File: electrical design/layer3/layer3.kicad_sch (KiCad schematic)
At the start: 10 parts, among them U1 TEENSY 4.0

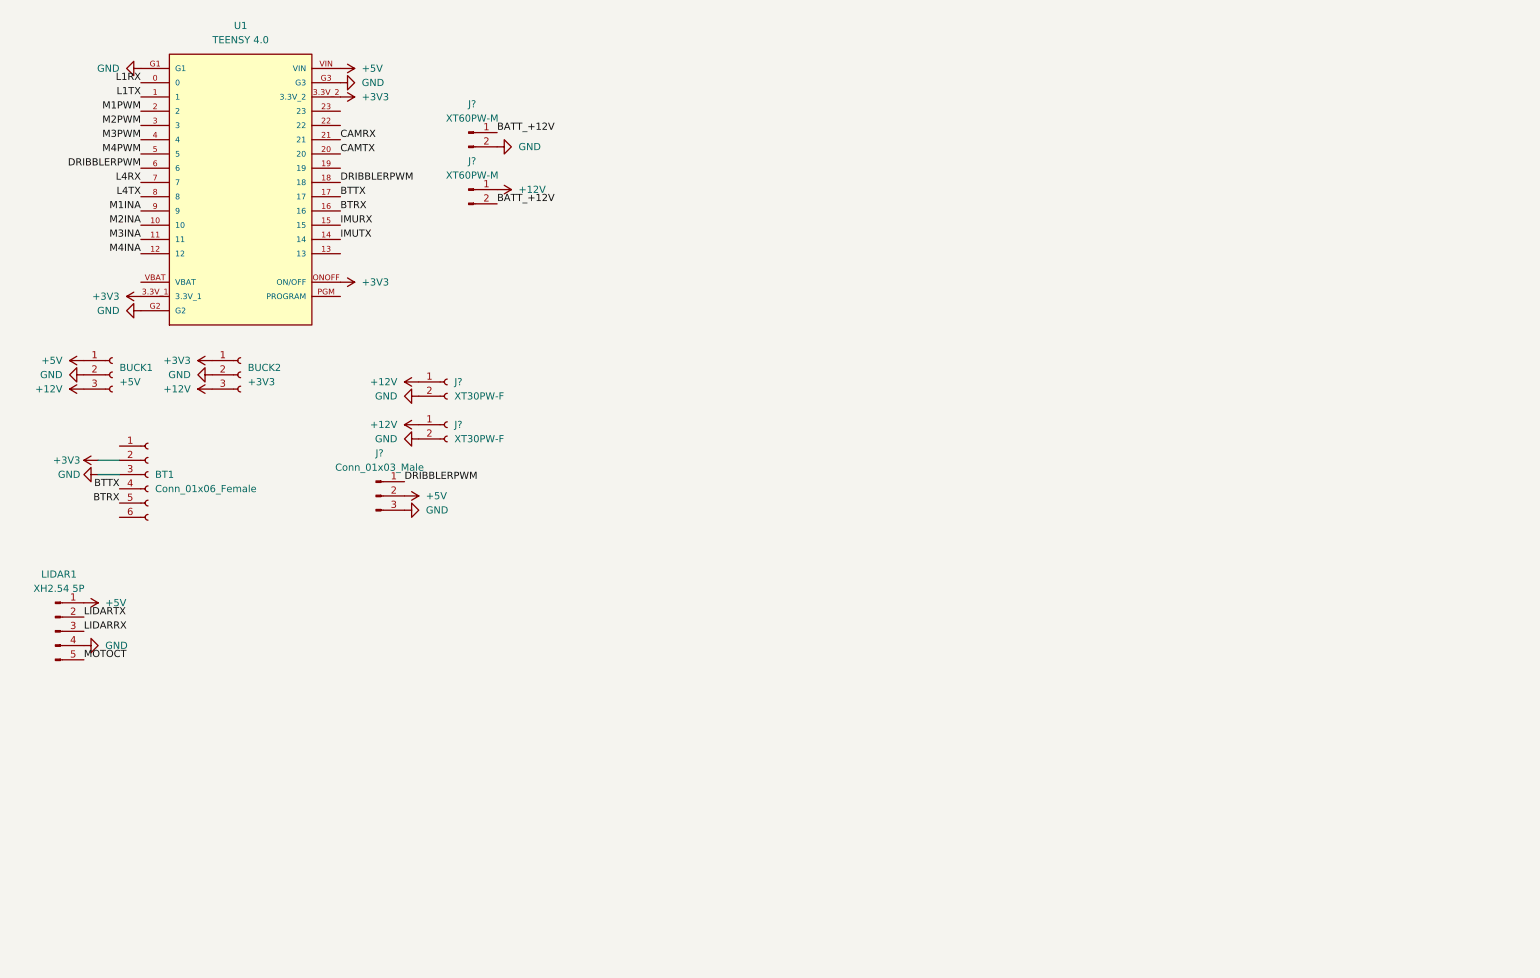
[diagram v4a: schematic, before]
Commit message: almost final layer 3 pcb design
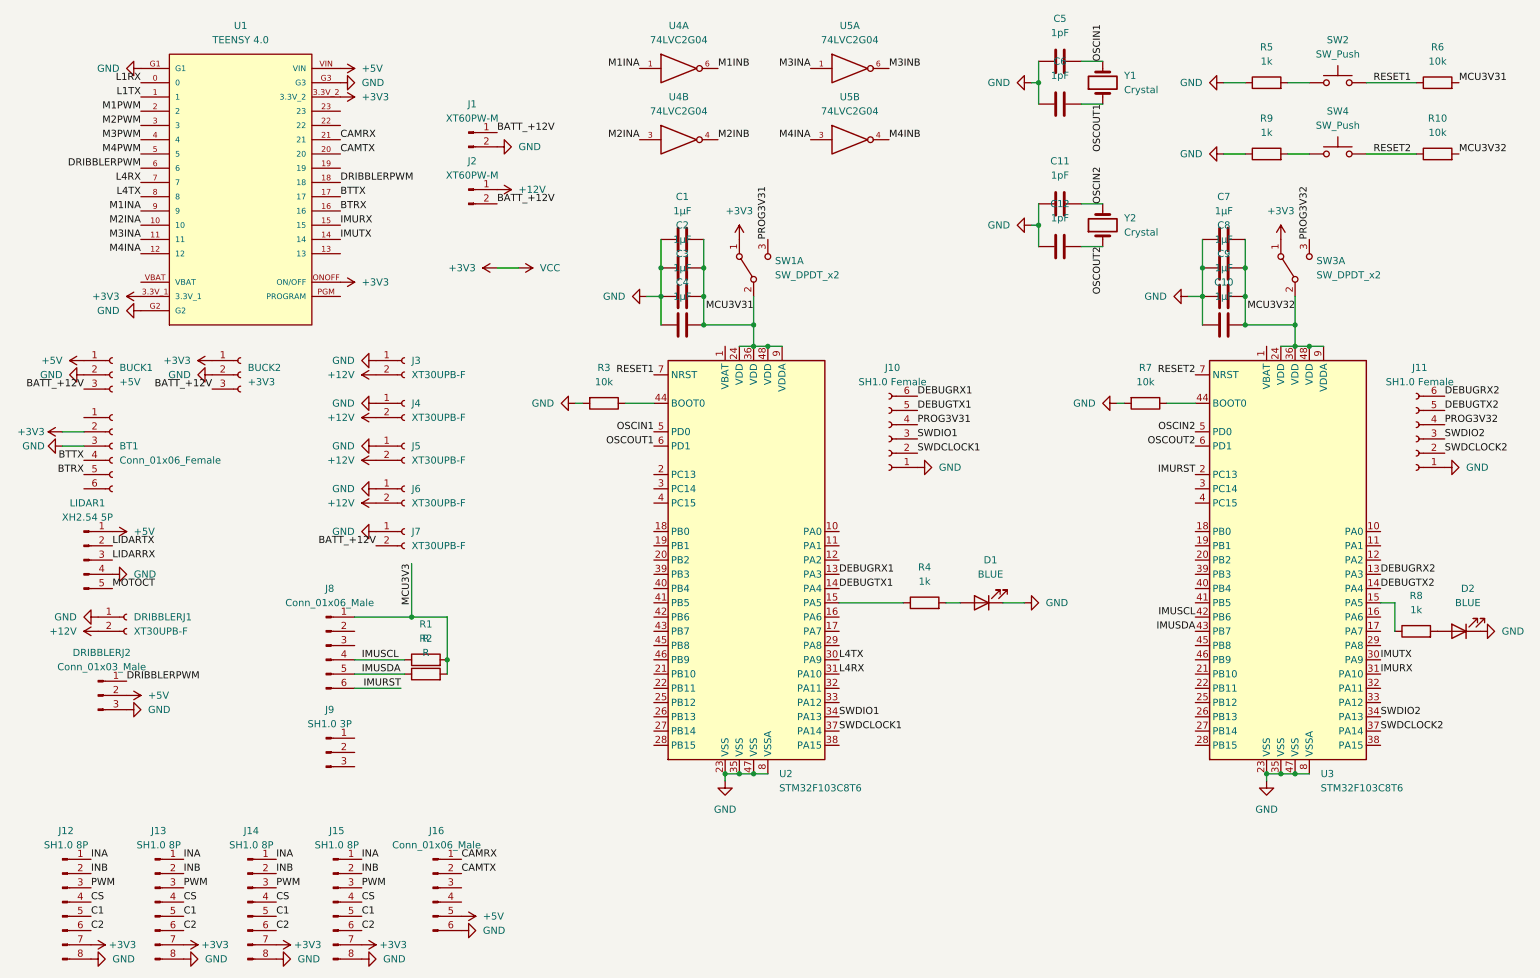
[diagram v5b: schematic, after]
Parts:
- removed J?: XT30PW-F, symbol Connector:Conn_01x02_Female
- added C1, C10, C2, C3, C4, C7, C8, C9: 1μF, Capacitor_SMD:C_0603_1608Metric, symbol Device:C
- added C11, C12, C5, C6: 1pF, Capacitor_SMD:C_0603_1608Metric, symbol Device:C
- added D1, D2: BLUE, Diode_SMD:D_0603_1608Metric, symbol Device:LED
- added J10, J11: SH1.0 Female, Connector_JST:JST_SH_BM06B-SRSS-TB_1x06-1MP_P1.00mm_Vertical, symbol Connector:Conn_01x06_Female
- added J12, J13, J14, J15: SH1.0 8P, Connector_JST:JST_SH_BM08B-SRSS-TB_1x08-1MP_P1.00mm_Vertical, symbol Connector:Conn_01x08_Male
- added J16: Conn_01x06_Male, Connector_JST:JST_GH_SM06B-GHS-TB_1x06-1MP_P1.25mm_Horizontal, symbol Connector:Conn_01x06_Male
- added J3, J4, J5, J6, J7: XT30UPB-F, Connector_AMASS:AMASS_XT30UPB-F_1x02_P5.0mm_Vertical, symbol Connector:Conn_01x02_Female
- added J8: Conn_01x06_Male, Connector_PinHeader_2.54mm:PinHeader_1x06_P2.54mm_Vertical, symbol Connector:Conn_01x06_Male
- added J9: SH1.0 3P, Connector_JST:JST_SH_SM03B-SRSS-TB_1x03-1MP_P1.00mm_Horizontal, symbol Connector:Conn_01x03_Male
- added R1, R2: R, Resistor_SMD:R_0603_1608Metric, symbol Device:R
- added R10, R3, R6, R7: 10k, Resistor_SMD:R_0603_1608Metric, symbol Device:R
- added R4, R5, R8, R9: 1k, Resistor_SMD:R_0603_1608Metric, symbol Device:R
- added SW1, SW3: SW_DPDT_x2, Switches:SWITCH_SPDT_PTH_11.6X4.0MM_LOCK, symbol Switch:SW_DPDT_x2
- added SW2, SW4: SW_Push, Button_Switch_SMD:SW_Push_SPST_NO_Alps_SKRK, symbol Switch:SW_Push
- added U2, U3: STM32F103C8T6, Package_QFP:LQFP-48_7x7mm_P0.5mm, symbol MCU_ST_STM32F1:STM32F103C8Tx
- added U4, U5: 74LVC2G04, Package_TO_SOT_SMD:SOT-23-6, symbol 74xGxx:74LVC2G04
- added Y1, Y2: Crystal, Crystal:Crystal_SMD_5032-2Pin_5.0x3.2mm, symbol Device:Crystal
- BT1: footprint (none) -> Connector_PinHeader_2.54mm:PinHeader_1x06_P2.54mm_Vertical
- BUCK1, BUCK2: footprint Connectors:1X03_LOCK -> Connector_PinHeader_2.54mm:PinHeader_1x03_P2.54mm_Vertical
- DRIBBLERJ1: renamed from J?; value XT30PW-F -> XT30UPB-F; footprint (none) -> Connector_AMASS:AMASS_XT30UPB-F_1x02_P5.0mm_Vertical
- DRIBBLERJ2: renamed from J?; footprint (none) -> Connector_PinHeader_2.54mm:PinHeader_1x03_P2.54mm_Vertical
- LIDAR1: footprint (none) -> Connector_JST:JST_XH_B5B-XH-AM_1x05_P2.50mm_Vertical
- gave numbers to parts that had none: 2
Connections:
- net +12V: now also DRIBBLERJ1.2 (Pin_2), J3.2 (Pin_2), J4.2 (Pin_2), J5.2 (Pin_2), J6.2 (Pin_2); no longer BUCK1.3 (Pin_3), BUCK2.3 (Pin_3), DRIBBLERJ1.1 (Pin_1)
- net +3V3: now also J12.7 (Pin_7), J13.7 (Pin_7), J14.7 (Pin_7), J15.7 (Pin_7), SW1.1 (A), SW3.1 (A), U4.5 (VCC), U4.5 (VCC), U5.5 (VCC), U5.5 (VCC)
- net +5V: now also J16.5 (Pin_5)
- net BATT_+12V: now also BUCK1.3 (Pin_3), BUCK2.3 (Pin_3), J7.2 (Pin_2)
- net CAMRX: now also J16.1 (Pin_1)
- net CAMTX: now also J16.2 (Pin_2)
- net GND: now also DRIBBLERJ1.1 (Pin_1), C1.1, C10.1, C11.1, C12.1, C2.1, C3.1, C4.1, C5.1, C6.1, C7.1, C8.1, C9.1, D1.1 (K), D2.1 (K), J10.1 (Pin_1), J11.1 (Pin_1), J12.8 (Pin_8), J13.8 (Pin_8), J14.8 (Pin_8), J15.8 (Pin_8), J16.6 (Pin_6), J3.1 (Pin_1), J4.1 (Pin_1), J5.1 (Pin_1), J6.1 (Pin_1), J7.1 (Pin_1), R3.2, R5.1, R7.2, R9.1, U2.23 (VSS), U2.35 (VSS), U2.47 (VSS), U2.8 (VSSA), U3.23 (VSS), U3.35 (VSS), U3.47 (VSS), U3.8 (VSSA), U4.2 (GND), U4.2 (GND), U5.2 (GND), U5.2 (GND); no longer DRIBBLERJ1.2 (Pin_2)
- net IMURX: now also U3.31 (PA10)
- net IMUTX: now also U3.30 (PA9)
- net L4RX: now also U2.31 (PA10)
- net L4TX: now also U2.30 (PA9)
- net M1INA: now also U4.1
- net M2INA: now also U4.3
- net M3INA: now also U5.1
- net M4INA: now also U5.3
- new net: R5.2, SW2.1
- new net: D1.2 (A), R4.2
- new net: R4.1, U2.15 (PA5)
- new net: R3.1, U2.44 (BOOT0)
- new net: R8.1, U3.15 (PA5)
- new net: R7.1, U3.44 (BOOT0)
- new net: R9.2, SW4.1
- new net: D2.2 (A), R8.2
- new net C1: J12.5 (Pin_5), J13.5 (Pin_5), J14.5 (Pin_5), J15.5 (Pin_5)
- new net C2: J12.6 (Pin_6), J13.6 (Pin_6), J14.6 (Pin_6), J15.6 (Pin_6)
- new net CS: J12.4 (Pin_4), J13.4 (Pin_4), J14.4 (Pin_4), J15.4 (Pin_4)
- new net DEBUGRX1: J10.6 (Pin_6), U2.13 (PA3)
- new net DEBUGRX2: J11.6 (Pin_6), U3.13 (PA3)
- new net DEBUGTX1: J10.5 (Pin_5), U2.14 (PA4)
- new net DEBUGTX2: J11.5 (Pin_5), U3.14 (PA4)
- new net IMURST: J8.6 (Pin_6), U3.2 (PC13)
- new net IMUSCL: J8.4 (Pin_4), R1.1, U3.42 (PB6)
- new net IMUSDA: J8.5 (Pin_5), R2.1, U3.43 (PB7)
- new net INA: J12.1 (Pin_1), J13.1 (Pin_1), J14.1 (Pin_1), J15.1 (Pin_1)
- new net INB: J12.2 (Pin_2), J13.2 (Pin_2), J14.2 (Pin_2), J15.2 (Pin_2)
- new net M1INB: U4.6
- new net M2INB: U4.4
- new net M3INB: U5.6
- new net M4INB: U5.4
- new net MCU3V3: J8.1 (Pin_1), R1.2, R2.2
- new net MCU3V31: C1.2, C2.2, C3.2, C4.2, R6.2, SW1.2 (B), U2.24 (VDD), U2.36 (VDD), U2.48 (VDD), U2.9 (VDDA)
- new net MCU3V32: C10.2, C7.2, C8.2, C9.2, R10.2, SW3.2 (B), U3.24 (VDD), U3.36 (VDD), U3.48 (VDD), U3.9 (VDDA)
- new net OSCIN1: C5.2, U2.5 (PD0), Y1.2
- new net OSCIN2: C11.2, U3.5 (PD0), Y2.2
- new net OSCOUT1: C6.2, U2.6 (PD1), Y1.1
- new net OSCOUT2: C12.2, U3.6 (PD1), Y2.1
- new net PROG3V31: J10.4 (Pin_4), SW1.3 (C)
- new net PROG3V32: J11.4 (Pin_4), SW3.3 (C)
- new net PWM: J12.3 (Pin_3), J13.3 (Pin_3), J14.3 (Pin_3), J15.3 (Pin_3)
- new net RESET1: R6.1, SW2.2, U2.7 (NRST)
- new net RESET2: R10.1, SW4.2, U3.7 (NRST)
- new net SWDCLOCK1: J10.2 (Pin_2), U2.37 (PA14)
- new net SWDCLOCK2: J11.2 (Pin_2), U3.37 (PA14)
- new net SWDIO1: J10.3 (Pin_3), U2.34 (PA13)
- new net SWDIO2: J11.3 (Pin_3), U3.34 (PA13)
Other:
- moved on the sheet: BT1, DRIBBLERJ1, DRIBBLERJ2, LIDAR1

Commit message: update l1, l3, and driver pcbs
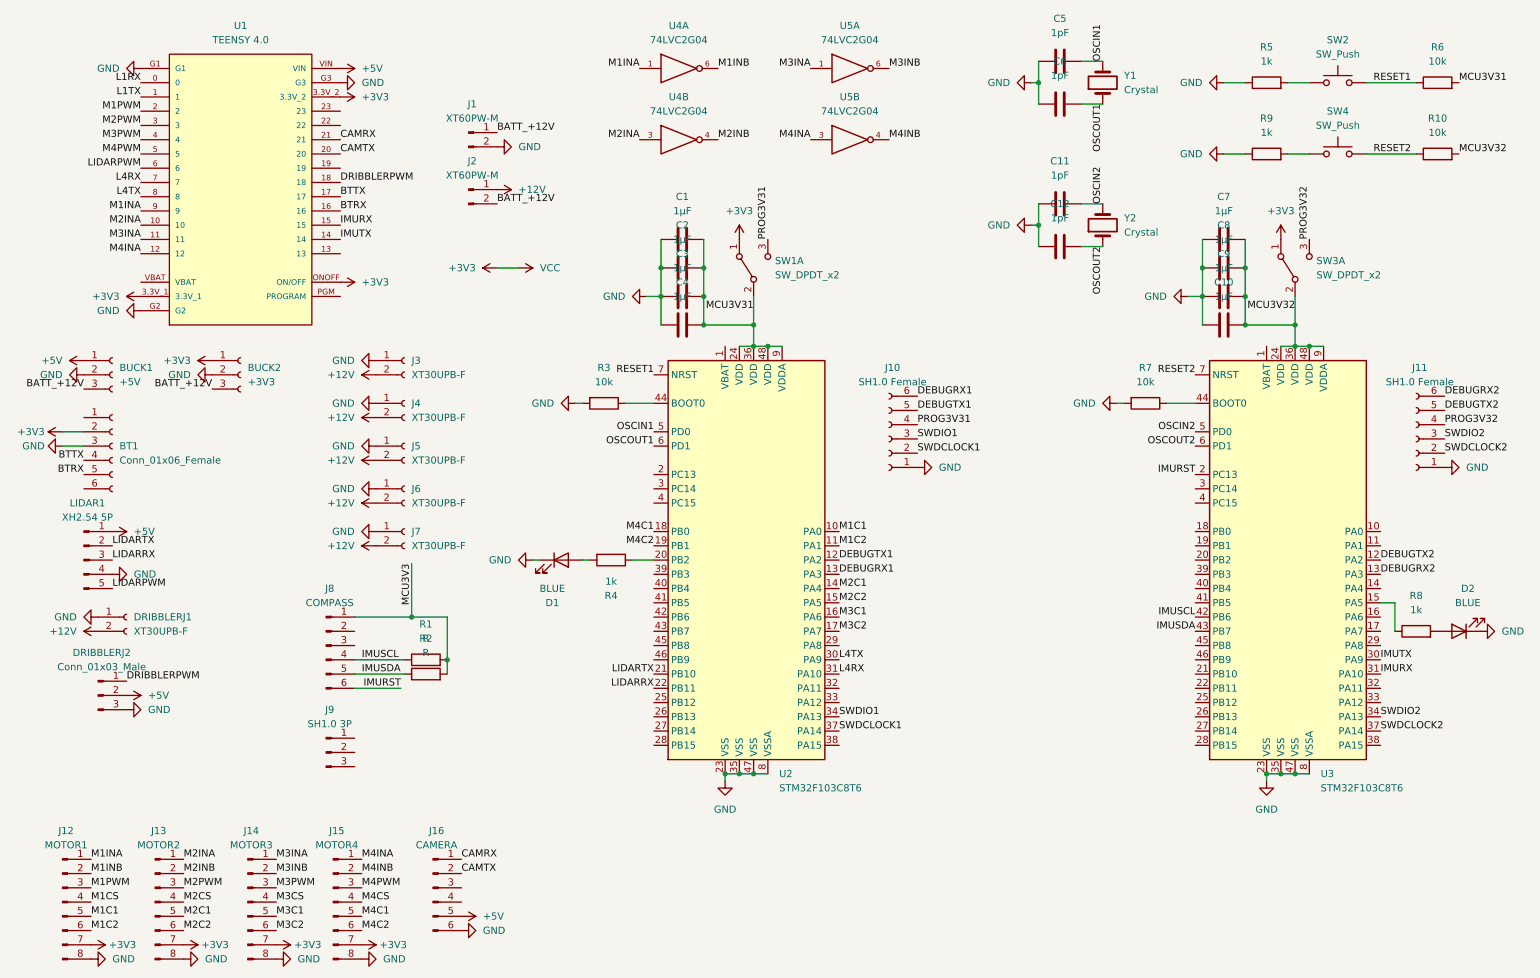
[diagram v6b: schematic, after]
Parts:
- BT1: footprint Connector_PinHeader_2.54mm:PinHeader_1x06_P2.54mm_Vertical -> Connector_PinSocket_2.54mm:PinSocket_1x06_P2.54mm_Horizontal
- J1, J2: footprint (none) -> XT60PW-M:AMASS_XT60PW-M
- J12: value SH1.0 8P -> MOTOR1
- J13: value SH1.0 8P -> MOTOR2
- J14: value SH1.0 8P -> MOTOR3
- J15: value SH1.0 8P -> MOTOR4
- J16: value Conn_01x06_Male -> CAMERA
- J8: value Conn_01x06_Male -> COMPASS
- LIDAR1: footprint Connector_JST:JST_XH_B5B-XH-AM_1x05_P2.50mm_Vertical -> Connector_JST:JST_XH_B5B-XH-A_1x05_P2.50mm_Vertical
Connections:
- net +12V: now also J7.2 (Pin_2)
- net BATT_+12V: no longer J7.2 (Pin_2)
- net DEBUGTX1: now also U2.12 (PA2); no longer U2.14 (PA4)
- net DEBUGTX2: now also U3.12 (PA2); no longer U3.14 (PA4)
- net DRIBBLERPWM: no longer U1.6
- net LIDARRX: now also U2.22 (PB11)
- net LIDARTX: now also U2.21 (PB10)
- net M1INA: now also J12.1 (Pin_1)
- net M1INB: now also J12.2 (Pin_2)
- net M1PWM: now also J12.3 (Pin_3)
- net M2INA: now also J13.1 (Pin_1)
- net M2INB: now also J13.2 (Pin_2)
- net M2PWM: now also J13.3 (Pin_3)
- net M3INA: now also J14.1 (Pin_1)
- net M3INB: now also J14.2 (Pin_2)
- net M3PWM: now also J14.3 (Pin_3)
- net M4INA: now also J15.1 (Pin_1)
- net M4INB: now also J15.2 (Pin_2)
- net M4PWM: now also J15.3 (Pin_3)
- net M1C1: now reaches U2.10 (PA0)
- net M1C1: now also J12.5 (Pin_5)
- net M1C2: now reaches U2.11 (PA1)
- net M1C2: now also J12.6 (Pin_6)
- net at R4.1: now also U2.20 (PB2); no longer U2.15 (PA5)
- net M3C1: now reaches U2.16 (PA6)
- net M3C1: now also J14.5 (Pin_5)
- net M3C2: now reaches U2.17 (PA7)
- net M3C2: now also J14.6 (Pin_6)
- net M4C1: now reaches U2.18 (PB0)
- net M4C1: now also J15.5 (Pin_5)
- net M4C2: now reaches U2.19 (PB1)
- net M4C2: now also J15.6 (Pin_6)
- removed net C1: J12.5 (Pin_5), J13.5 (Pin_5), J14.5 (Pin_5), J15.5 (Pin_5)
- removed net C2: J12.6 (Pin_6), J13.6 (Pin_6), J14.6 (Pin_6), J15.6 (Pin_6)
- removed net CS: J12.4 (Pin_4), J13.4 (Pin_4), J14.4 (Pin_4), J15.4 (Pin_4)
- removed net INA: J12.1 (Pin_1), J13.1 (Pin_1), J14.1 (Pin_1), J15.1 (Pin_1)
- removed net INB: J12.2 (Pin_2), J13.2 (Pin_2), J14.2 (Pin_2), J15.2 (Pin_2)
- net MOTOCT renamed LIDARPWM
- net LIDARPWM: now also U1.6
- removed net PWM: J12.3 (Pin_3), J13.3 (Pin_3), J14.3 (Pin_3), J15.3 (Pin_3)
- new net M1CS: J12.4 (Pin_4)
- new net M2C1: J13.5 (Pin_5), U2.14 (PA4)
- new net M2C2: J13.6 (Pin_6), U2.15 (PA5)
- new net M2CS: J13.4 (Pin_4)
- new net M3CS: J14.4 (Pin_4)
- new net M4CS: J15.4 (Pin_4)
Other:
- moved on the sheet: D1, R4
